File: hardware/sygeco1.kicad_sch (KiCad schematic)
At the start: 23 parts, among them J1 SSD1306_module, J2 AVR-ISP-6, SW1 SW_Push_DPDT, SW2 SW_Push_DPDT, U1 ATtiny85-20PU

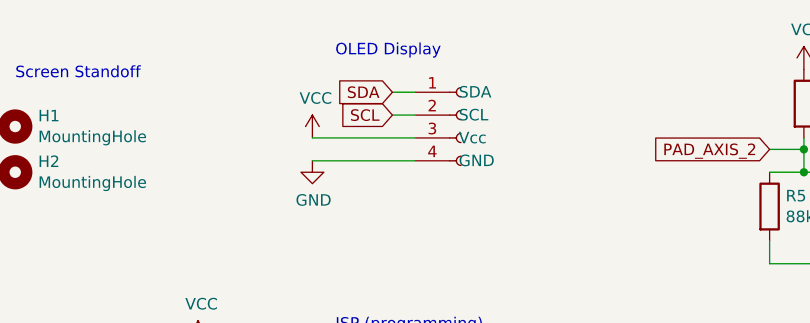
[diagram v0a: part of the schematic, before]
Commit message: random cleaning, mostly kicad updating its stuff
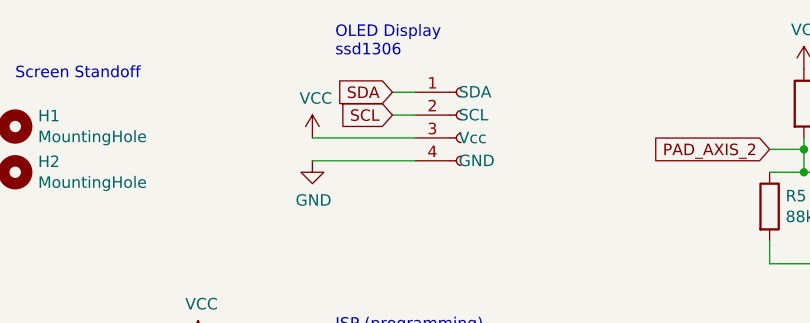
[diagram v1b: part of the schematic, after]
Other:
- note added: "OLED Display ssd1306"
- note removed: "OLED Display"
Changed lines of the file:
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@@
-(kicad_sch (version 20210621) (generator eeschema)
+(kicad_sch (version 20211123) (generator eeschema)
   (paper "User" 210.795 148.488)
   (title_block
@@
     (company "Sylphide Consulting")
   )
-  (junction (at 111.76 36.83) (diameter 0) (color 0 0 0 0))
-  (junction (at 59.69 104.14) (diameter 0) (color 0 0 0 0))
-  (junction (at 46.99 119.38) (diameter 0) (color 0 0 0 0))
-  (junction (at 55.88 104.14) (diameter 0) (color 0 0 0 0))
-  (junction (at 111.76 34.29) (diameter 0) (color 0 0 0 0))
-  (junction (at 153.67 41.91) (diameter 0) (color 0 0 0 0))
-  (junction (at 40.64 106.68) (diameter 0) (color 0 0 0 0))
-  (junction (at 59.69 119.38) (diameter 0) (color 0 0 0 0))
-  (junction (at 175.26 36.83) (diameter 0) (color 0 0 0 0))
-  (junction (at 171.45 36.83) (diameter 0) (color 0 0 0 0))
+  (junction (at 111.76 34.29) (diameter 0) (color 0 0 0 0)
+  )
+  (junction (at 171.45 36.83) (diameter 0) (color 0 0 0 0)
+  )
+  (junction (at 153.67 41.91) (diameter 0) (color 0 0 0 0)
+  )
+  (junction (at 59.69 104.14) (diameter 0) (color 0 0 0 0)
+  )
+  (junction (at 59.69 119.38) (diameter 0) (color 0 0 0 0)
+  )
+  (junction (at 40.64 106.68) (diameter 0) (color 0 0 0 0)
+  )
+  (junction (at 111.76 36.83) (diameter 0) (color 0 0 0 0)
+  )
+  (junction (at 55.88 104.14) (diameter 0) (color 0 0 0 0)
+  )
+  (junction (at 175.26 36.83) (diameter 0) (color 0 0 0 0)
+  )
+  (junction (at 46.99 119.38) (diameter 0) (color 0 0 0 0)
+  )
   (no_connect (at 11.43 55.88))
   (no_connect (at 50.8 99.06))
@@
     (effects (font (size 1.27 1.27)) (justify left bottom))
   )
-  (text "OLED Display" (at 59.69 24.13 0)
+  (text "OLED Display\nssd1306" (at 59.69 24.13 0)
     (effects (font (size 1.27 1.27)) (justify left bottom))
   )

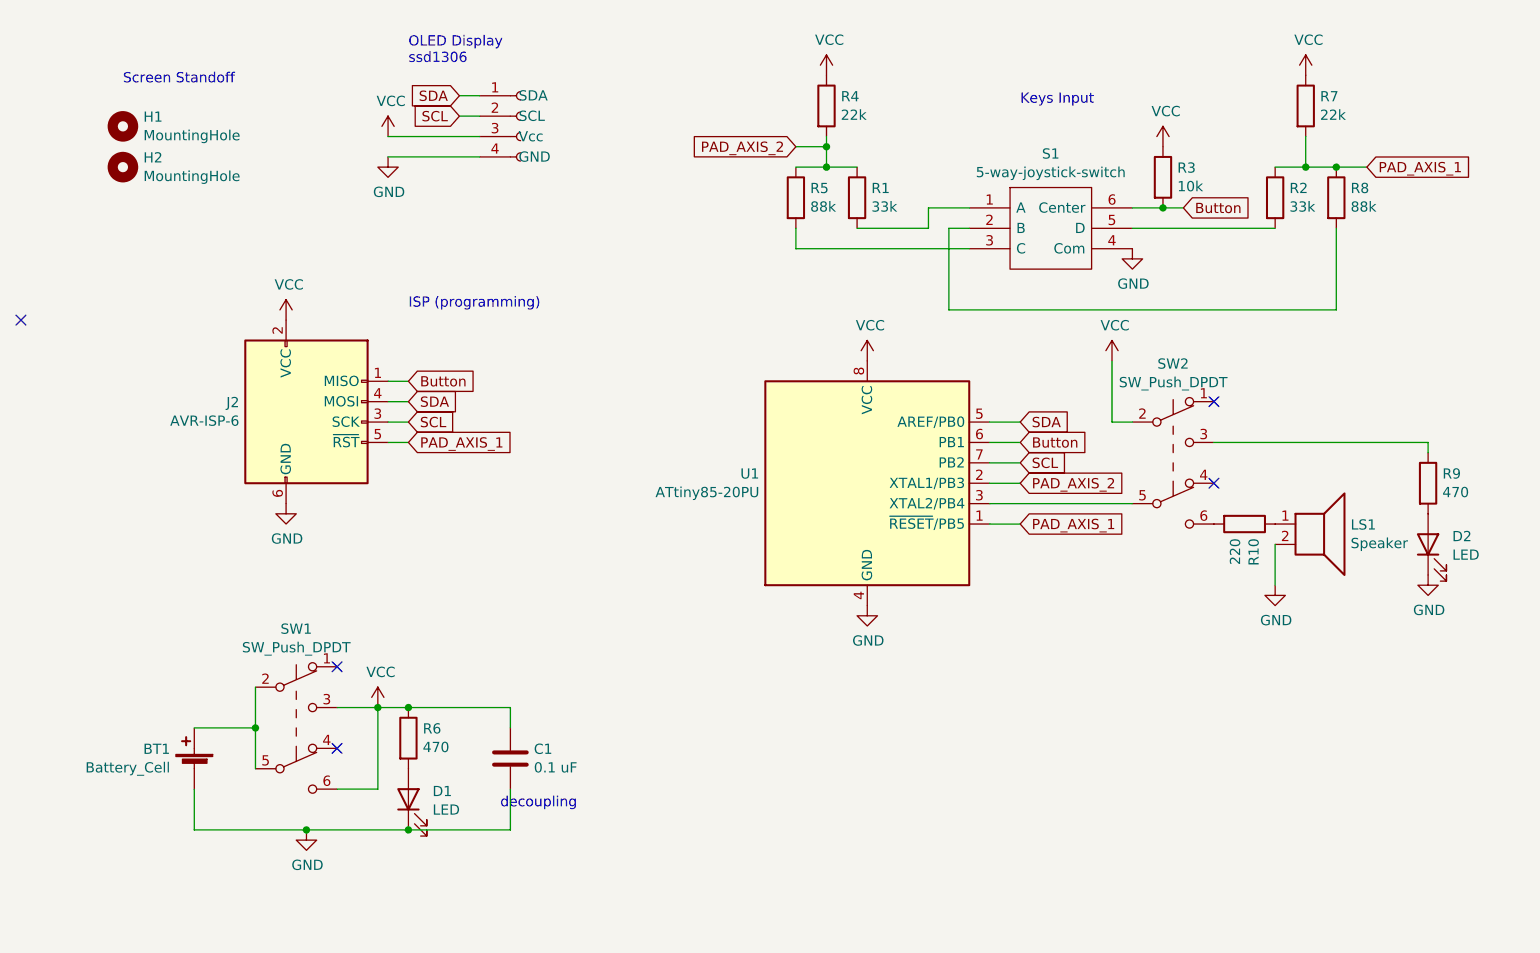
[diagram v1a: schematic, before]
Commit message: Add some (silicone) pads. pcb: cleaning all errors/warnings
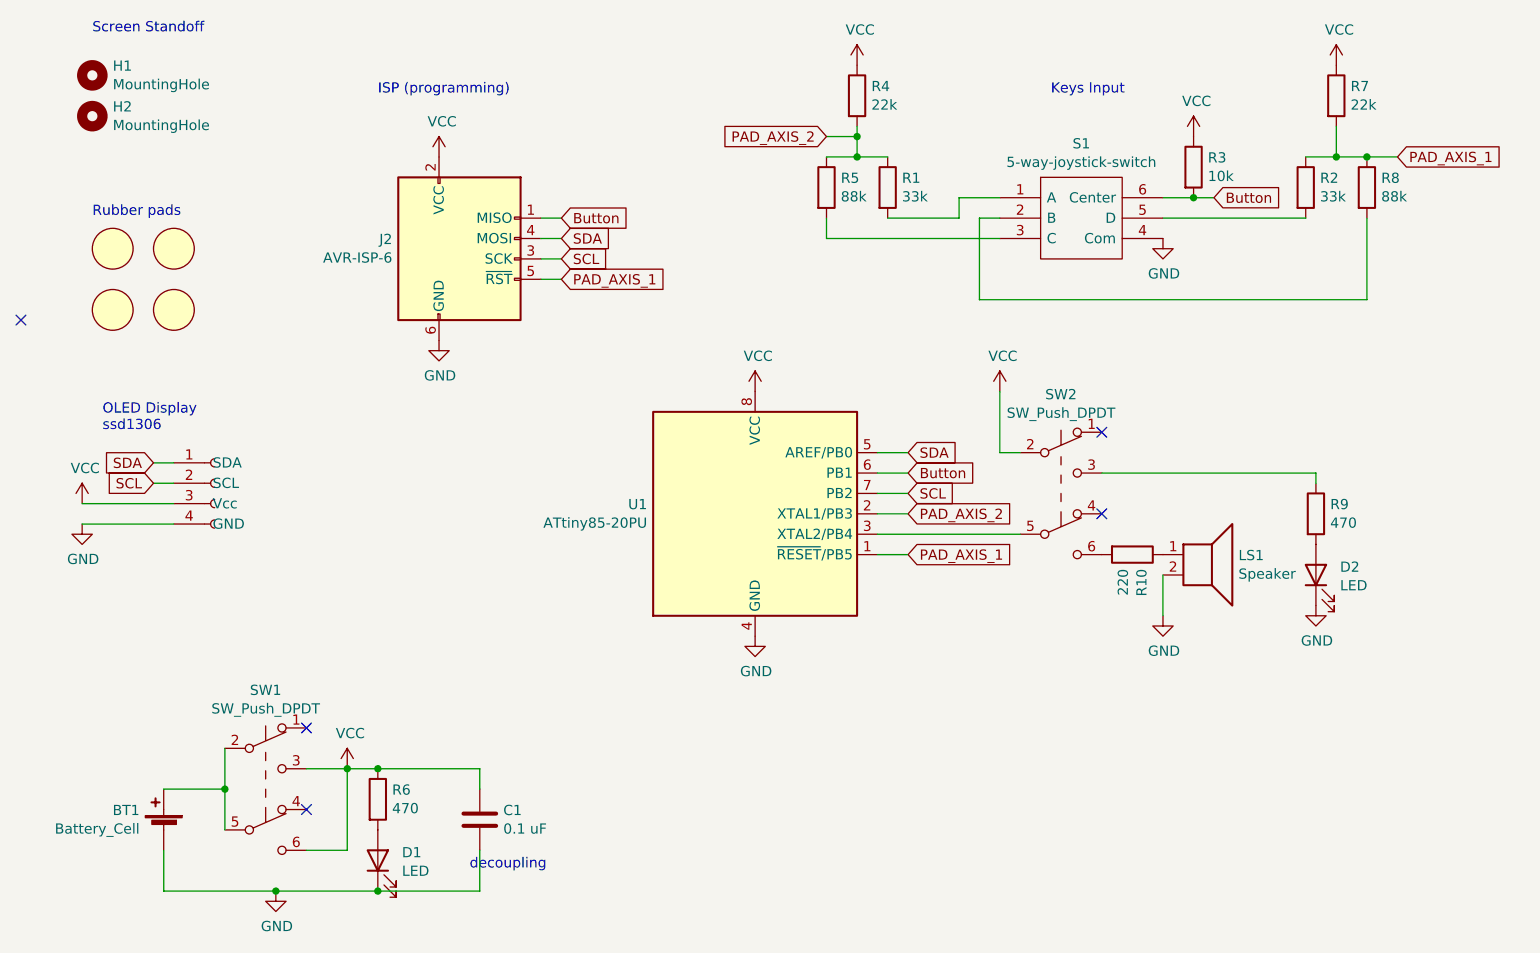
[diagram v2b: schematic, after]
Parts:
- added RP1, RP2, RP3, RP4: silicone_rubber_pad, sygeco:silicone_rubber_pad, symbol sygeco1_symbols:silicone_rubber_pad
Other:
- note added: "Rubber pads"
- moved on the sheet: BT1, C1, D1, D2, H1, H2, J2, LS1, R1, R10, R2, R3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

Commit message: Fix attiny85 symbol + all errors/warnings. Seems like my symbol was obsolate..(?)
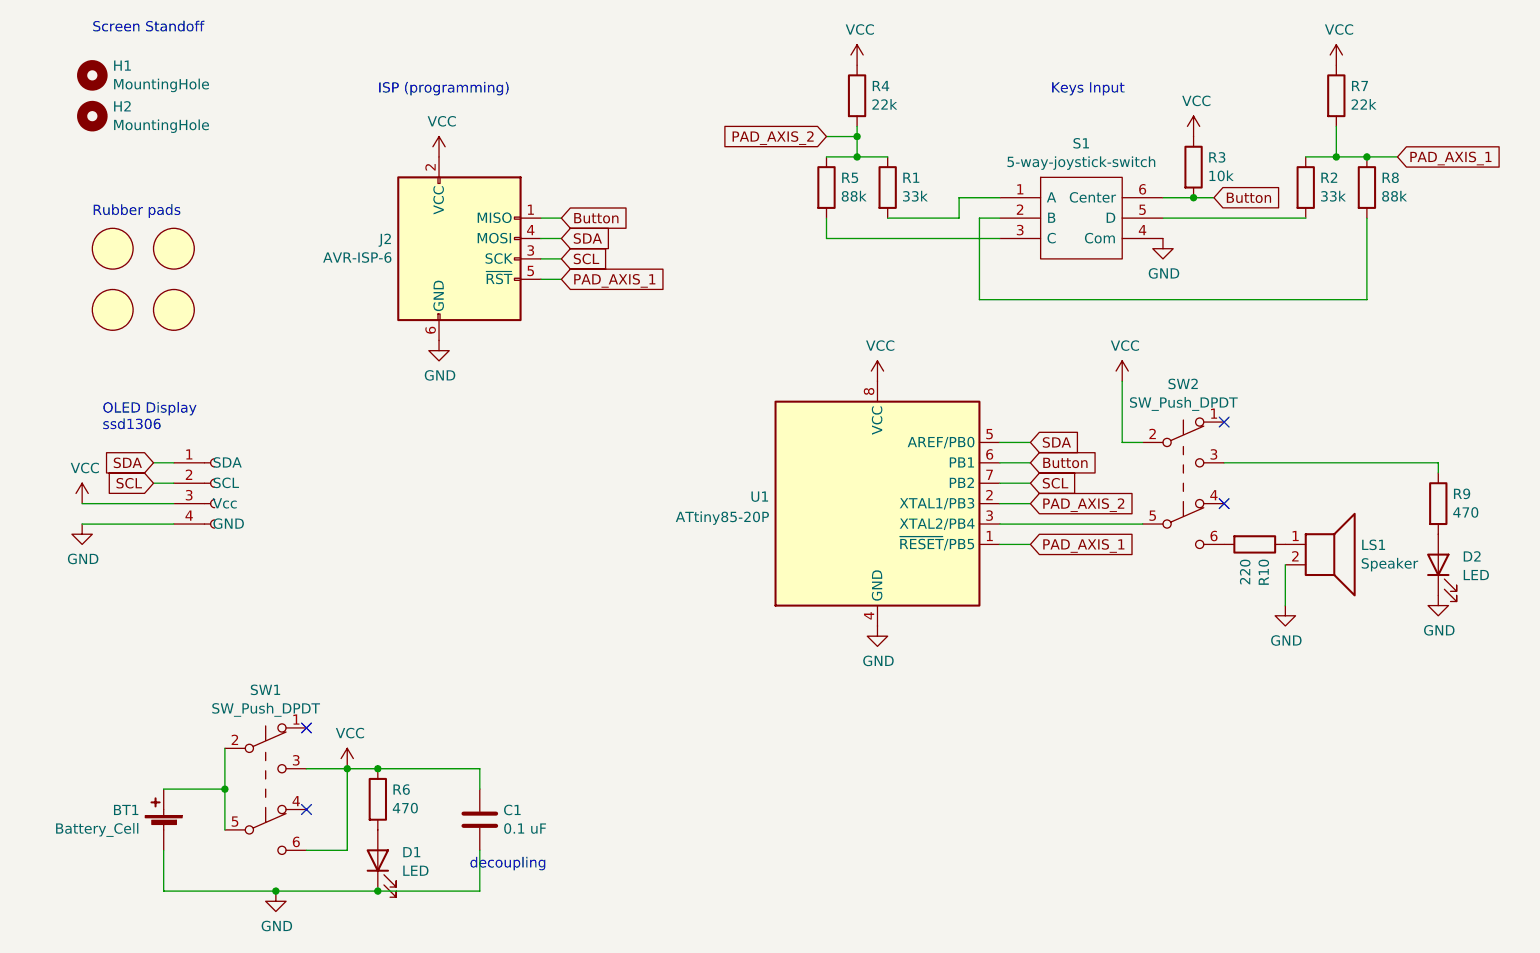
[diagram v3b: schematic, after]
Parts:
- removed U1: ATtiny85-20PU, Package_DIP:DIP-8_W7.62mm_Socket_LongPads, symbol MCU_Microchip_ATtiny:ATtiny85-20PU
- added U1: ATtiny85-20P, Package_DIP:DIP-8_W7.62mm, symbol MCU_Microchip_ATtiny:ATtiny85-20P
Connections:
- net Button: now also U1.6 (PB1)
- net GND: now also U1.4 (GND)
- net PAD_AXIS_1: now also U1.1 (~{RESET}/PB5)
- net PAD_AXIS_2: now also U1.2 (XTAL1/PB3)
- net SCL: now also U1.7 (PB2)
- net SDA: now also U1.5 (AREF/PB0)
- net VCC: now also U1.8 (VCC)
- net at SW2.5 (B): now also U1.3 (XTAL2/PB4)
- no-connect marks 5 -> 4
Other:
- moved on the sheet: D2, LS1, R10, R9, SW2

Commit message: Add dual footprints for the MCU. This way you can put either a dip8 or a sop8. Quite useful in those times of parts shortage.
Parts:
- U1: footprint Package_DIP:DIP-8_W7.62mm -> sygeco1:dual-dip8-sop8
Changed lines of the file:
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@@
       (effects (font (size 1.27 1.27)) (justify right))
     )
-    (property "Footprint" "Package_DIP:DIP-8_W7.62mm" (id 2) (at 118.11 78.74 0)
+    (property "Footprint" "sygeco1:dual-dip8-sop8" (id 2) (at 118.11 78.74 0)
       (effects (font (size 1.27 1.27) italic) hide)
     )
@@
     )
     (path "/25d9567d-ae96-495e-b9a6-57b1f43d7140"
-      (reference "U1") (unit 1) (value "ATtiny85-20P") (footprint "Package_DIP:DIP-8_W7.62mm")
-    )
-  )
+      (reference "U1") (unit 1) (value "ATtiny85-20P") (footprint "sygeco1:dual-dip8-sop8")
+    )
+  )
